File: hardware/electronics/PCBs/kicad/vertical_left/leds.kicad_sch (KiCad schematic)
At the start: 7 parts

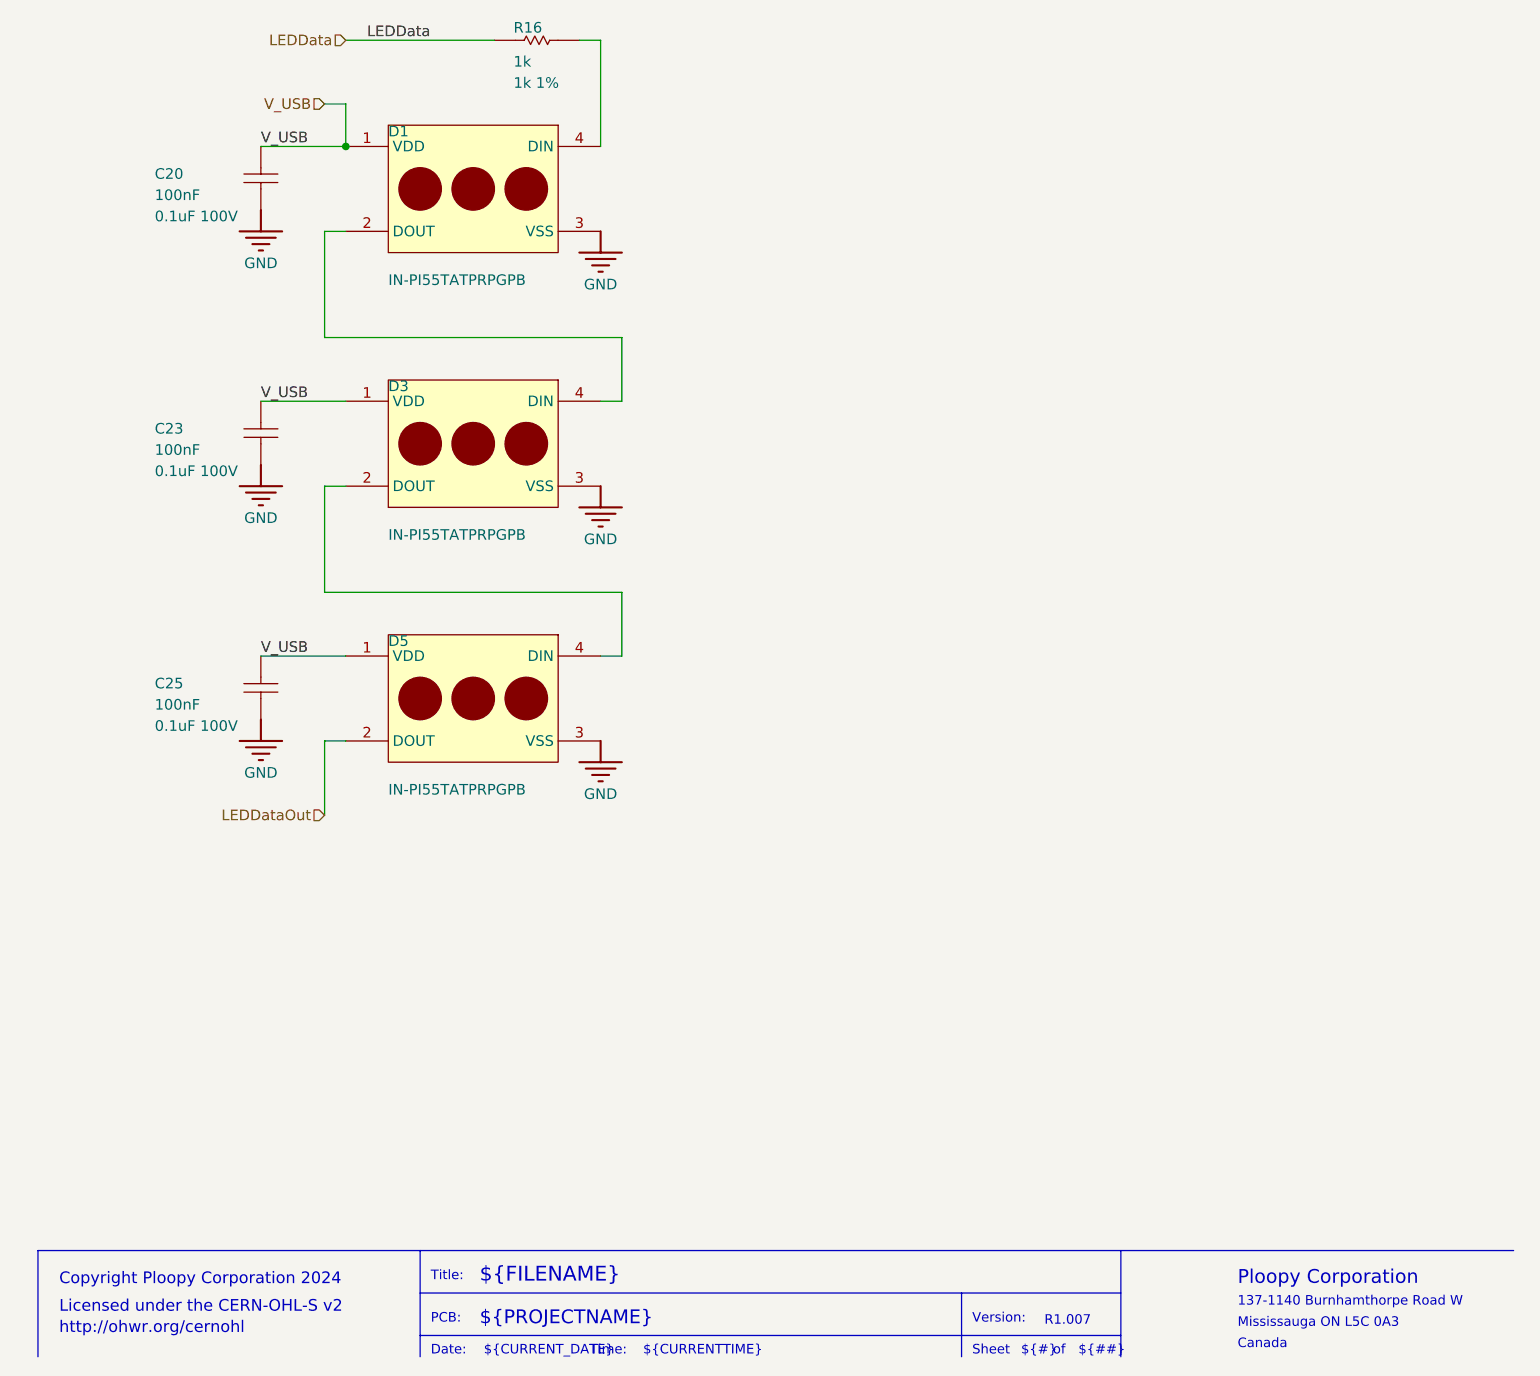
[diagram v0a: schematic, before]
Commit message: Vertical neopixels
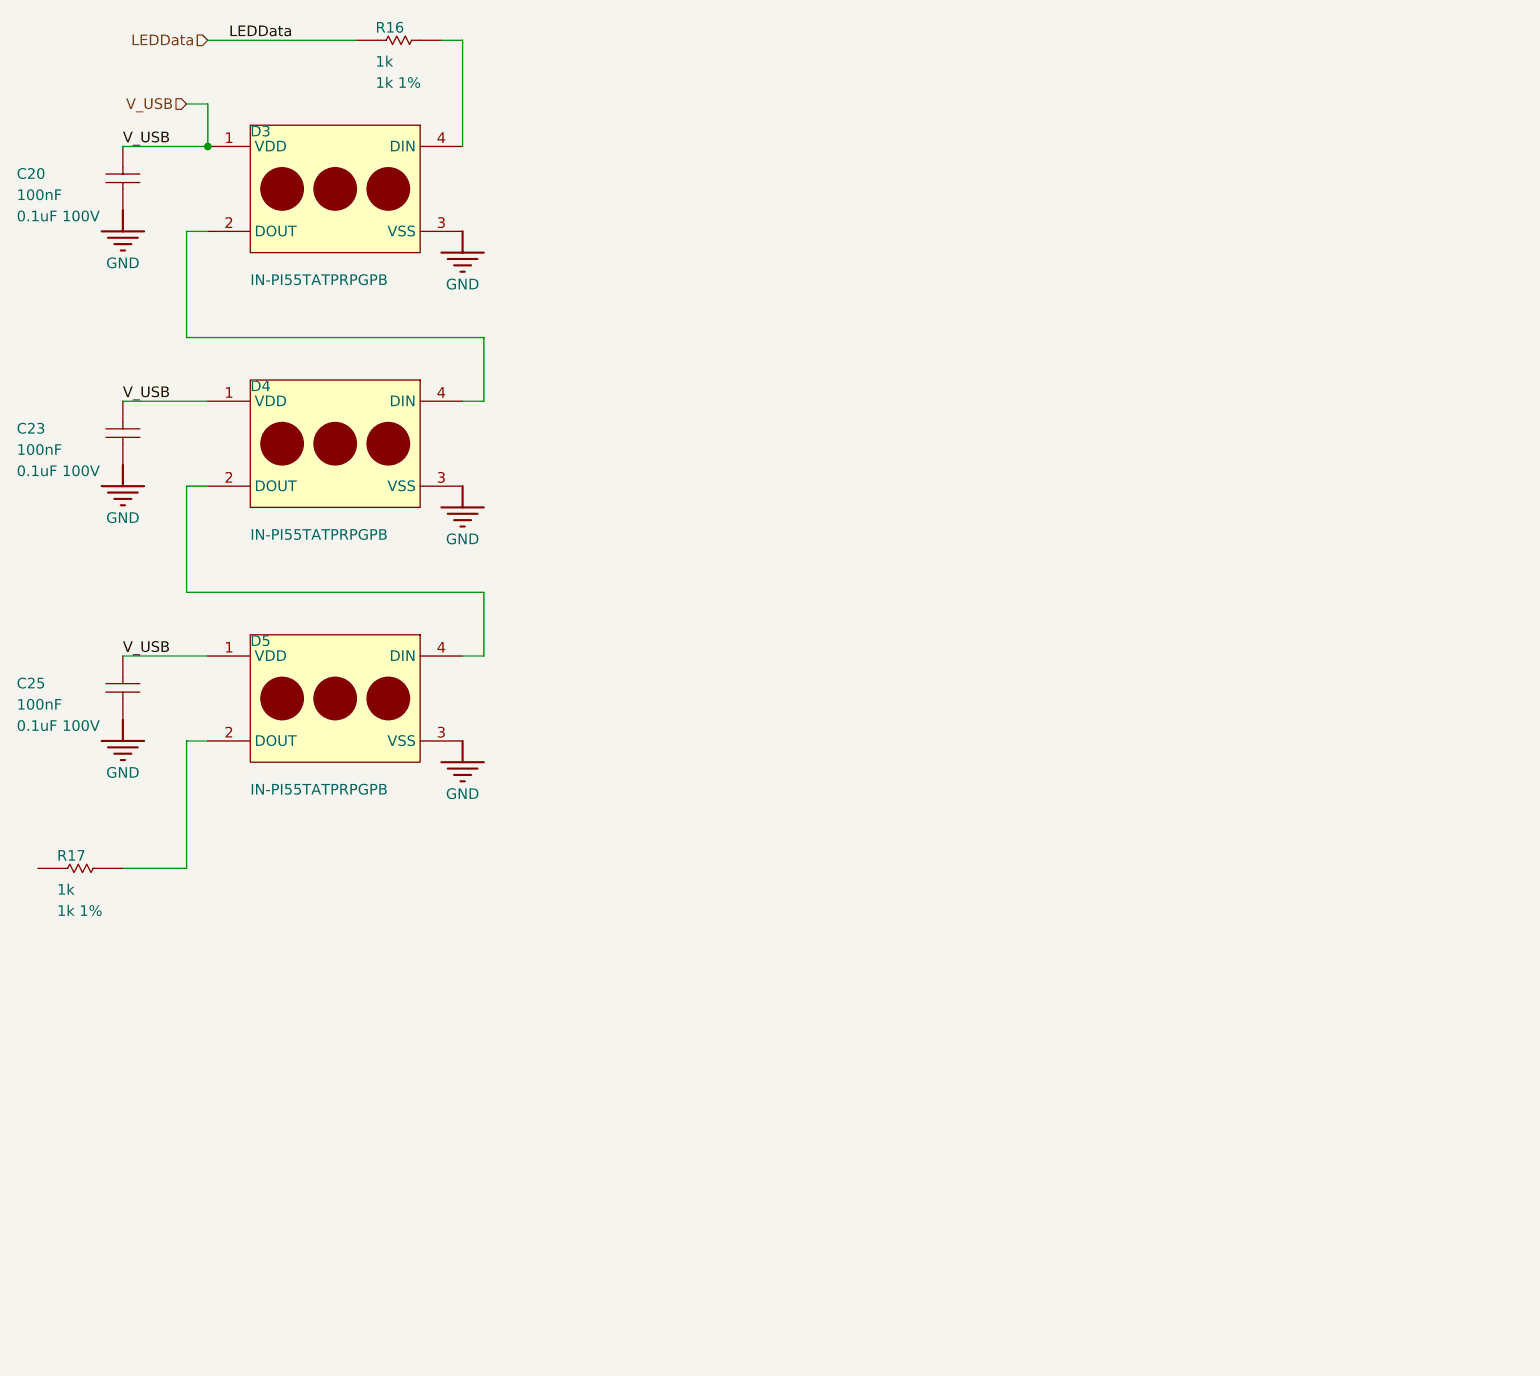
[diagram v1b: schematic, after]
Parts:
- removed D1: IN-PI55TATPRPGPB, IN-PI55TATPRPGPB, symbol LEDs:LED_0_IN-PI55TATPRPGPB_LEDs.SchLib
- added D4: IN-PI55TATPRPGPB, IN-PI55TATPRPGPB, symbol LEDs:LED_0_IN-PI55TATPRPGPB_LEDs.SchLib
- added R17: 1k, Resistor_SMD:R_0805_2012Metric, symbol Chip_Passives:LED_2_Res 1k 1% 0805_Chip_Passives.SchLib
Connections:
- net GND: now also D4.3 (VSS)
- net V_USB: now also D4.1 (VDD)
- net at D5.4 (DIN): now also D4.2 (DOUT); no longer D3.2 (DOUT)
- net at D3.4 (DIN): now also R16.1
- net LEDDataOut: no longer names the net of D5.2 (DOUT)
- net LEDDataOut: now also R17.1
- new net: D3.2 (DOUT), D4.4 (DIN)
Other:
- note removed: "${##}"
- note removed: "${#}"
- note removed: "${CURRENTTIME}"
- note removed: "${CURRENT_DATE}"
- note removed: "${FILENAME}"
- note removed: "${PROJECTNAME}"
- note removed: "${REVISION}"
- note removed: "137-1140 Burnhamthorpe Road W"
- note removed: "Canada"
- note removed: "Copyright Ploopy Corporation 2024"
- note removed: "Date:"
- note removed: "Licensed under the CERN-OHL-S v2"
- note removed: "Mississauga ON L5C 0A3"
- note removed: "PCB:"
- note removed: "Ploopy Corporation"
- note removed: "Sheet"
- note removed: "Time:"
- note removed: "Title:"
- note removed: "Version:"
- note removed: "http://ohwr.org/cernohl"
- note removed: "of"
- company: Ploopy Corporation -> (none)

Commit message: PCB revs. Add vertical rgb leds. Fix sensor cutout
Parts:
- D3, D4, D5: footprint IN-PI55TATPRPGPB -> LED_SMD:LED_WS2812B_PLCC4_5.0x5.0mm_P3.2mm
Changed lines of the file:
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@@
 			)
 		)
-		(property "Footprint" "IN-PI55TATPRPGPB"
+		(property "Footprint" "LED_SMD:LED_WS2812B_PLCC4_5.0x5.0mm_P3.2mm"
 			(at 133.35 101.6 0)
 			(hide yes)
@@
 			)
 		)
-		(property "Footprint" "IN-PI55TATPRPGPB"
+		(property "Footprint" "LED_SMD:LED_WS2812B_PLCC4_5.0x5.0mm_P3.2mm"
 			(at 133.35 71.12 0)
 			(hide yes)
@@
 			)
 		)
-		(property "Footprint" "IN-PI55TATPRPGPB"
+		(property "Footprint" "LED_SMD:LED_WS2812B_PLCC4_5.0x5.0mm_P3.2mm"
 			(at 133.35 132.08 0)
 			(hide yes)
